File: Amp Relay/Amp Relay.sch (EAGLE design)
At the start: 17 parts, among them IC1 LM358D, J1 OSTTA024163, J2 SJ-3523-SMT-TR, J3 SJ-3523-SMT-TR, Q1 BC849SMD, U1 G5LE-1A4_DC5

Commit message: aux ground and terminal block soldermask fix
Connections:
- removed net N$7: J2.1, J3.1
- net GND: now also J2.1, J3.1
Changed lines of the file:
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@@
 <pinref part="GND5" gate="1" pin="GND"/>
+</segment>
+<segment>
+<pinref part="J3" gate="G$1" pin="1"/>
+<pinref part="J2" gate="G$1" pin="1"/>
+<wire x1="-38.1" y1="45.72" x2="-12.7" y2="45.72" width="0.1524" layer="91"/>
+<label x="-27.94" y="45.72" size="1.778" layer="95"/>
 </segment>
 </net>
@@
 </segment>
 </net>
-<net name="N$7" class="0">
-<segment>
-<pinref part="J3" gate="G$1" pin="1"/>
-<pinref part="J2" gate="G$1" pin="1"/>
-<wire x1="-38.1" y1="45.72" x2="-12.7" y2="45.72" width="0.1524" layer="91"/>
-</segment>
-</net>

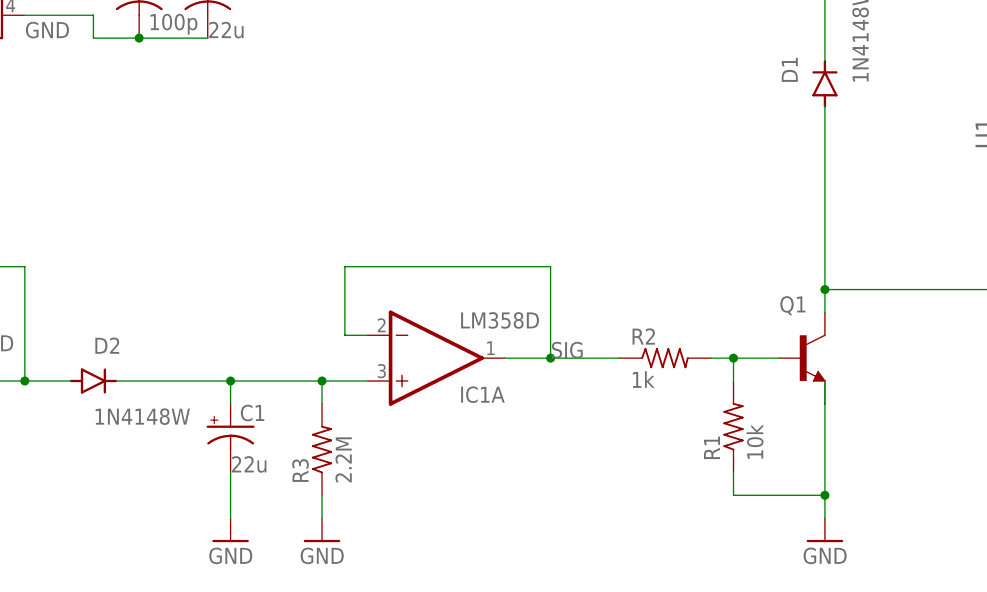
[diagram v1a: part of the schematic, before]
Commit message: added toggle switch, and cutouts for the aux ports
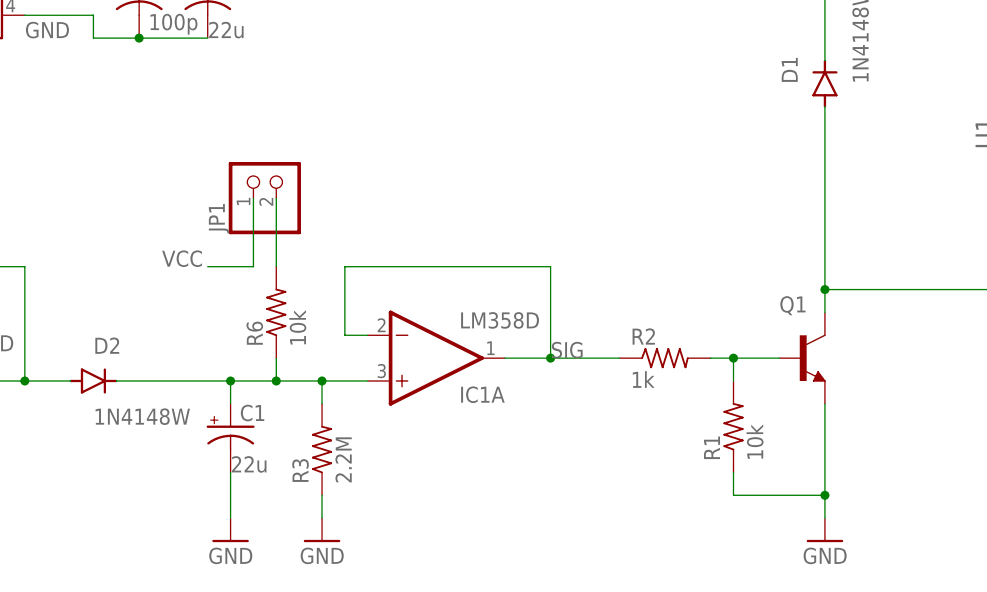
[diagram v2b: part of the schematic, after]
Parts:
- added JP1: (no value), pinhead:PINHD-1X2
- added R6: 10k, rcl:R-US_R1206
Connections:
- new net N$1: JP1.2, R6.2
- net N$5: now also R6.1
- net VCC: now also JP1.1
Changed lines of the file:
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@@
 <attribute name="C" value="22u"/>
 </part>
+<part name="JP1" library="pinhead" library_urn="urn:adsk.eagle:library:325" deviceset="PINHD-1X2" device="" package3d_urn="urn:adsk.eagle:package:22435/2"/>
+<part name="R6" library="rcl" library_urn="urn:adsk.eagle:library:334" deviceset="R-US_" device="R1206" package3d_urn="urn:adsk.eagle:package:23540/2" value="10k"/>
 </parts>
 <sheets>
@@
 <attribute name="C" x="50.8" y="58.42" size="1.778" layer="96"/>
 </instance>
+<instance part="JP1" gate="G$1" x="58.42" y="43.18" smashed="yes" rot="R90">
+<attribute name="NAME" x="52.705" y="36.83" size="1.778" layer="95" rot="R90"/>
+<attribute name="VALUE" x="63.5" y="36.83" size="1.778" layer="96" rot="R90"/>
+</instance>
+<instance part="R6" gate="G$1" x="58.42" y="27.94" smashed="yes" rot="R90">
+<attribute name="NAME" x="56.9214" y="24.13" size="1.778" layer="95" rot="R90"/>
+<attribute name="VALUE" x="61.722" y="24.13" size="1.778" layer="96" rot="R90"/>
+</instance>
 </instances>
 <busses>
@@
 <segment>
 <pinref part="GND1" gate="1" pin="GND"/>
-<pinref part="Q1" gate="G$1" pin="E"/>
-<wire x1="119.38" y1="17.78" x2="119.38" y2="20.32" width="0.1524" layer="91"/>
 <wire x1="119.38" y1="5.08" x2="119.38" y2="7.62" width="0.1524" layer="91"/>
 <pinref part="R1" gate="G$1" pin="1"/>
-<wire x1="119.38" y1="7.62" x2="119.38" y2="17.78" width="0.1524" layer="91"/>
 <wire x1="109.22" y1="10.16" x2="109.22" y2="7.62" width="0.1524" layer="91"/>
 <wire x1="109.22" y1="7.62" x2="119.38" y2="7.62" width="0.1524" layer="91"/>
+<pinref part="Q1" gate="G$1" pin="E"/>
+<wire x1="119.38" y1="17.78" x2="119.38" y2="7.62" width="0.1524" layer="91"/>
 <junction x="119.38" y="7.62"/>
 </segment>
@@
 <label x="20.32" y="27.94" size="1.778" layer="95"/>
 </segment>
+<segment>
+<pinref part="JP1" gate="G$1" pin="1"/>
+<wire x1="55.88" y1="40.64" x2="55.88" y2="33.02" width="0.1524" layer="91"/>
+<wire x1="55.88" y1="33.02" x2="50.8" y2="33.02" width="0.1524" layer="91"/>
+<label x="45.72" y="33.02" size="1.778" layer="95"/>
+</segment>
 </net>
 <net name="C" class="0">
@@
 <wire x1="53.34" y1="20.32" x2="53.34" y2="17.78" width="0.1524" layer="91"/>
 <pinref part="R3" gate="G$1" pin="2"/>
-<wire x1="53.34" y1="20.32" x2="63.5" y2="20.32" width="0.1524" layer="91"/>
+<wire x1="53.34" y1="20.32" x2="58.42" y2="20.32" width="0.1524" layer="91"/>
+<wire x1="58.42" y1="20.32" x2="63.5" y2="20.32" width="0.1524" layer="91"/>
 <wire x1="63.5" y1="20.32" x2="63.5" y2="17.78" width="0.1524" layer="91"/>
 <junction x="53.34" y="20.32"/>
@@
 <wire x1="63.5" y1="20.32" x2="68.58" y2="20.32" width="0.1524" layer="91"/>
 <junction x="63.5" y="20.32"/>
+<pinref part="R6" gate="G$1" pin="1"/>
+<wire x1="58.42" y1="22.86" x2="58.42" y2="20.32" width="0.1524" layer="91"/>
+<junction x="58.42" y="20.32"/>
 </segment>
 </net>
@@
 </segment>
 </net>
+<net name="N$1" class="0">
+<segment>
+<pinref part="R6" gate="G$1" pin="2"/>
+<pinref part="JP1" gate="G$1" pin="2"/>
+<wire x1="58.42" y1="33.02" x2="58.42" y2="40.64" width="0.1524" layer="91"/>
+</segment>
+</net>
